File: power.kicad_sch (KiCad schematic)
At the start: 53 parts, among them Q2 MMBT5551L, Q3 STN93003, U2 XL7005A, U3 ICW6215, U4 LM1117DT-3.3, X6 PWRBTN, X7 12V OUTLET, X8 5V OUTLET

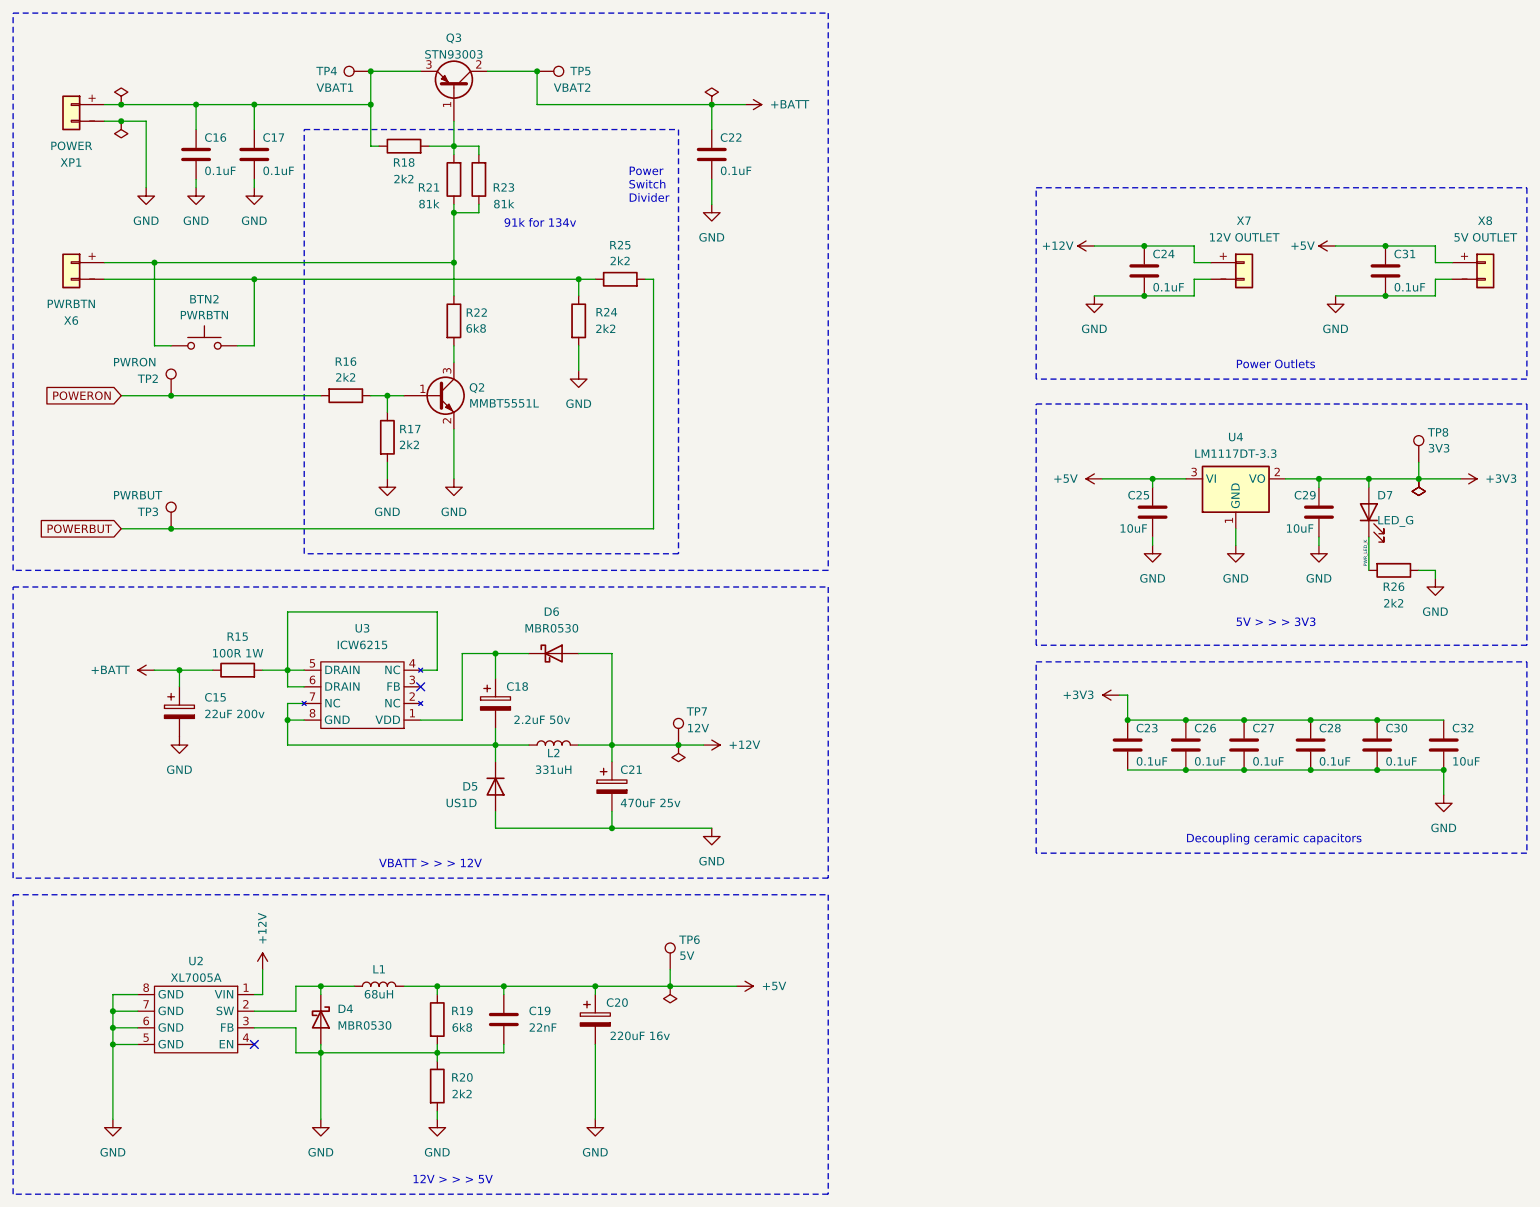
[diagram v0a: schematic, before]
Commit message: Fixed short cirquit, minors
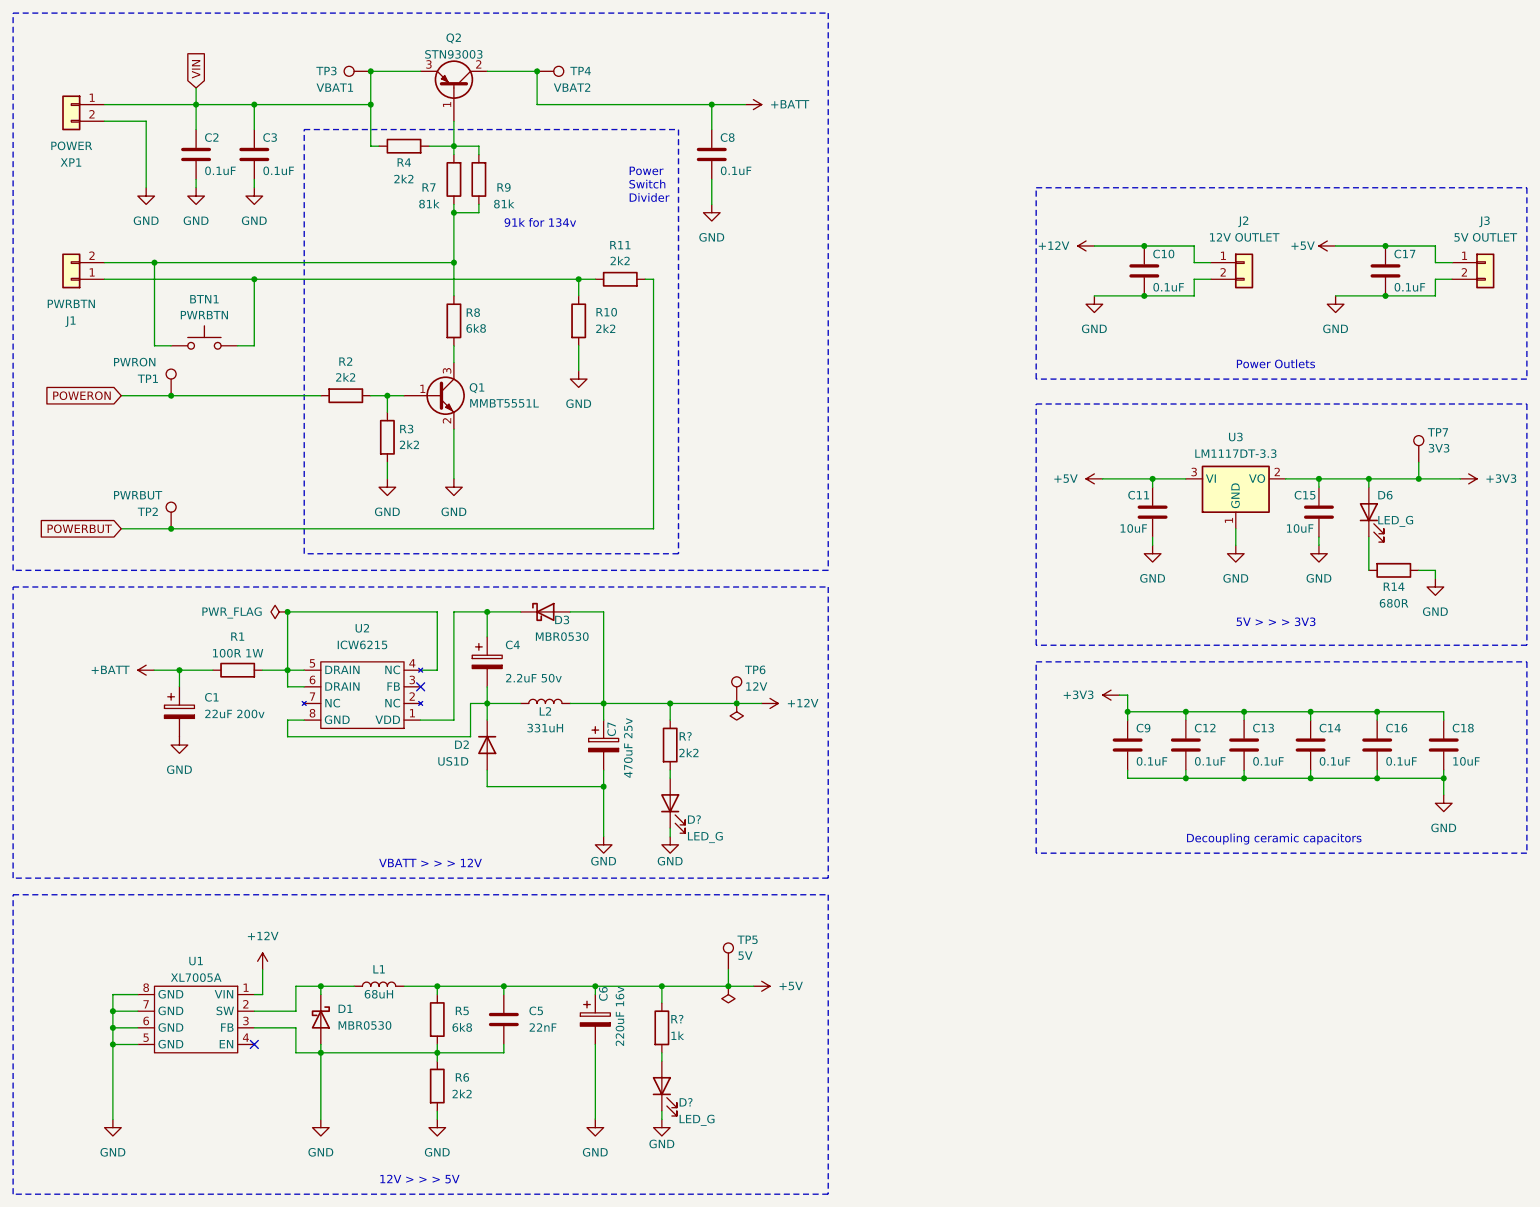
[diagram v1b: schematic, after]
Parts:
- removed X6: PWRBTN, symbol Connector_Generic:Conn_01x02
- removed X7: 12V OUTLET, symbol Connector_Generic:Conn_01x02
- removed X8: 5V OUTLET, symbol Connector_Generic:Conn_01x02
- added D? (x2): LED_G, LED_SMD:LED_0603_1608Metric, symbol Device:LED
- added J1: PWRBTN, symbol Connector_Generic:Conn_01x02
- added J2: 12V OUTLET, symbol Connector_Generic:Conn_01x02
- added J3: 5V OUTLET, symbol Connector_Generic:Conn_01x02
- added R?: 1k, Resistor_SMD:R_0603_1608Metric_Pad0.98x0.95mm_HandSolder, symbol Device:R
- added R?: 2k2, Resistor_SMD:R_0603_1608Metric_Pad0.98x0.95mm_HandSolder, symbol Device:R
- R14: renamed from R26; value 2k2 -> 680R
- renumbered BTN2 to BTN1, C15 to C1, C24 to C10, C25 to C11, C26 to C12, C27 to C13, C28 to C14, C29 to C15, C30 to C16, C31 to C17, C32 to C18, C16 to C2, C17 to C3, C18 to C4, C19 to C5, C20 to C6, C21 to C7, C22 to C8, C23 to C9, D4 to D1, D5 to D2, D6 to D3, D7 to D6, Q2 to Q1, Q3 to Q2, R15 to R1, R24 to R10, R25 to R11, R16 to R2, R17 to R3, R18 to R4, R19 to R5, R20 to R6, R21 to R7, R22 to R8, R23 to R9, TP2 to TP1, TP3 to TP2, TP4 to TP3, TP5 to TP4, TP6 to TP5, TP7 to TP6, TP8 to TP7, U2 to U1, U3 to U2, U4 to U3
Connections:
- net +12V: now also J2.1 (Pin_1), R?.1
- net +5V: now also J3.1 (Pin_1), R?.1
- net GND: now also XP1.2 (Pin_2), D?.1 (K), D?.1 (K), J2.2 (Pin_2), J3.2 (Pin_2); no longer XP1._ (Pin_2)
- net at C4.2, D2.1 (K), L2.1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: no longer U2.7 (NC)
- net at BTN1.1, R7.1, R8.1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: now also J1.2 (Pin_2)
- net VIN: now reaches C2.1, C3.1, Q2.3 (E), R4.1, TP3.1
- net VIN: now also XP1.1 (Pin_1); no longer XP1.+ (Pin_1)
- net at BTN1.2, R10.1, R11.1: now also J1.1 (Pin_1)
- net PWR_LED_K: no longer names the net of D6.1 (K), R14.2
- new net: D?.2 (A), R?.2 (x2)
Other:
- moved on the sheet: C4, C7, D2, D3, L2, TP5, TP6

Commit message: Fix mistakes
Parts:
- removed C1: 22uF 200v, Capacitor_SMD:CP_Elec_10x10, symbol Device:C_Polarized
- removed C10, C12, C13, C14, C16, C17, C9: 0.1uF, Capacitor_SMD:C_0603_1608Metric_Pad1.08x0.95mm_HandSolder, symbol Device:C
- removed C11, C18: 10uF, Capacitor_SMD:C_0603_1608Metric_Pad1.08x0.95mm_HandSolder, symbol Device:C
- removed C15: 10uF, Capacitor_SMD:C_0805_2012Metric, symbol Device:C
- removed C4: 2.2uF 50v, Capacitor_SMD:C_0805_2012Metric_Pad1.18x1.45mm_HandSolder, symbol Device:C_Polarized
- removed C5: 22nF, Capacitor_SMD:C_0603_1608Metric_Pad1.08x0.95mm_HandSolder, symbol Device:C
- removed C6: 220uF 16v, Capacitor_SMD:CP_Elec_6.3x7.7, symbol Device:C_Polarized
- removed C7: 470uF 25v, Capacitor_SMD:CP_Elec_10x10.5, symbol Device:C_Polarized
- removed D1, D3: MBR0530, Diode_SMD:D_SOD-123, symbol Diode:MBR0530
- removed D2: US1D, Diode_SMD:D_SMA, symbol Diode:US1D
- removed D6, D? (x2): LED_G, LED_SMD:LED_0603_1608Metric, symbol Device:LED
- removed J2: 12V OUTLET, symbol Connector_Generic:Conn_01x02
- removed J3: 5V OUTLET, symbol Connector_Generic:Conn_01x02
- removed L1: 68uH, Inductor_SMD:L_Bourns_SRP7028A_7.3x6.6mm, symbol Device:L
- removed L2: 331uH, Inductor_SMD:L_Bourns_SRR1208_12.7x12.7mm, symbol Device:L
- removed R1: 100R 1W, Resistor_SMD:R_2010_5025Metric_Pad1.40x2.65mm_HandSolder, symbol Device:R
- removed R14: 680R, Resistor_SMD:R_0402_1005Metric, symbol Device:R
- removed R5: 6k8, Resistor_SMD:R_0603_1608Metric_Pad0.98x0.95mm_HandSolder, symbol Device:R
- removed R6, R?: 2k2, Resistor_SMD:R_0603_1608Metric_Pad0.98x0.95mm_HandSolder, symbol Device:R
- removed R?: 1k, Resistor_SMD:R_0603_1608Metric_Pad0.98x0.95mm_HandSolder, symbol Device:R
- removed TP5: 5V, TestPoint:TestPoint_Pad_D2.0mm, symbol Connector:TestPoint
- removed TP6: 12V, TestPoint:TestPoint_Pad_D2.0mm, symbol Connector:TestPoint
- removed TP7: 3V3, TestPoint:TestPoint_Pad_D2.0mm, symbol Connector:TestPoint
- removed U1: XL7005A, Package_SO:SOP-8_3.9x4.9mm_P1.27mm, symbol 4shift:XL7005a
- removed U2: ICW6215, Package_SO:SOP-8_3.9x4.9mm_P1.27mm, symbol 4shift:ICW6215
- removed U3: LM1117DT-3.3, Package_TO_SOT_SMD:TO-252-3_TabPin2, symbol Regulator_Linear:LM1117DT-3.3
- C2, C3: value 0.1uF -> 470nF
- C8: value 0.1uF -> 10uF
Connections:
- no-connect marks 2 -> 0
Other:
- note removed: "12V > > > 5V"
- note removed: "5V > > > 3V3"
- note removed: "Decoupling ceramic capacitors"
- note removed: "Power Outlets"
- note removed: "VBATT > > > 12V"
- moved on the sheet: BTN1, C2, C3, C8, J1, Q1, Q2, R10, R11, R2, R3, R4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

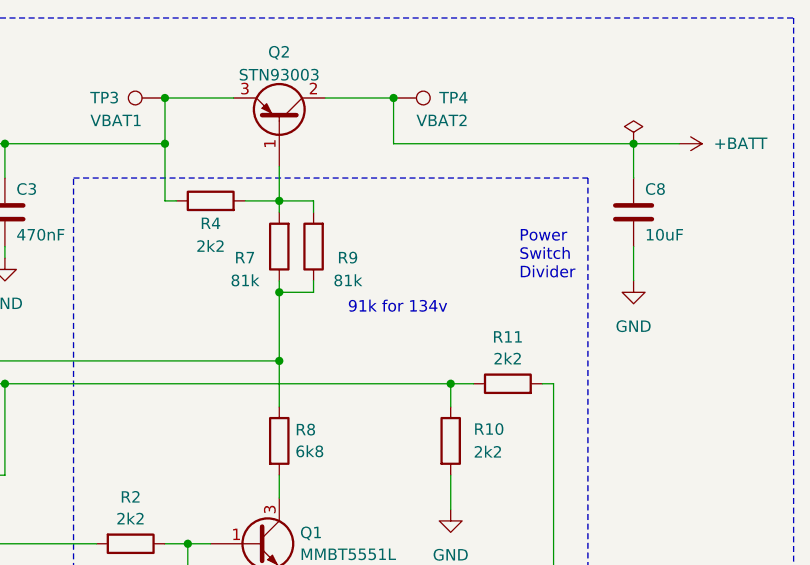
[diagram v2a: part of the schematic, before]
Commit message: Add drivers, stepdown on VIPER115, fixes
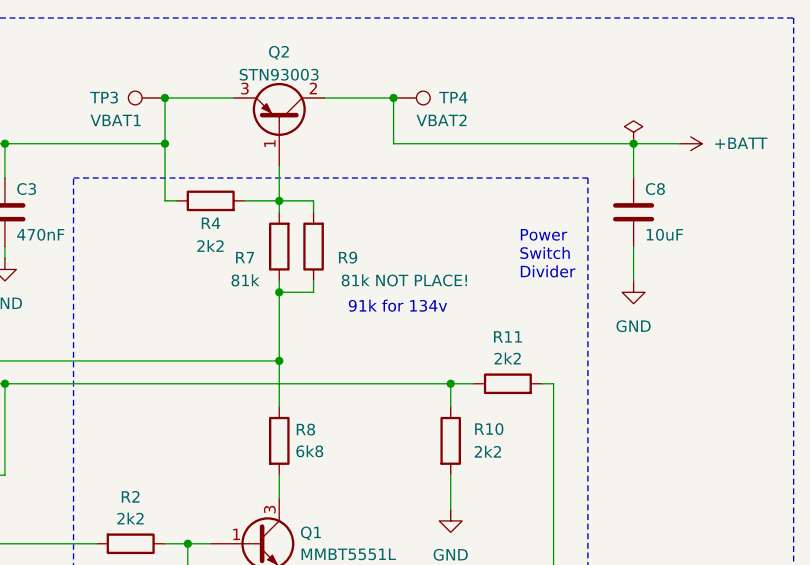
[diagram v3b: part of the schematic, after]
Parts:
- R9: value 81k -> 81k NOT PLACE!
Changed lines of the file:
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@@
       (effects (font (size 1.27 1.27)))
     )
-    (property "Value" "81k" (at 162.56 88.9 0)
+    (property "Value" "81k NOT PLACE!" (at 168.91 88.9 0)
       (effects (font (size 1.27 1.27)))
     )
